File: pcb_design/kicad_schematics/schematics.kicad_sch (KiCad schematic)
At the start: 10 parts, among them IC1 PIC24FJ64GA702-I_SO

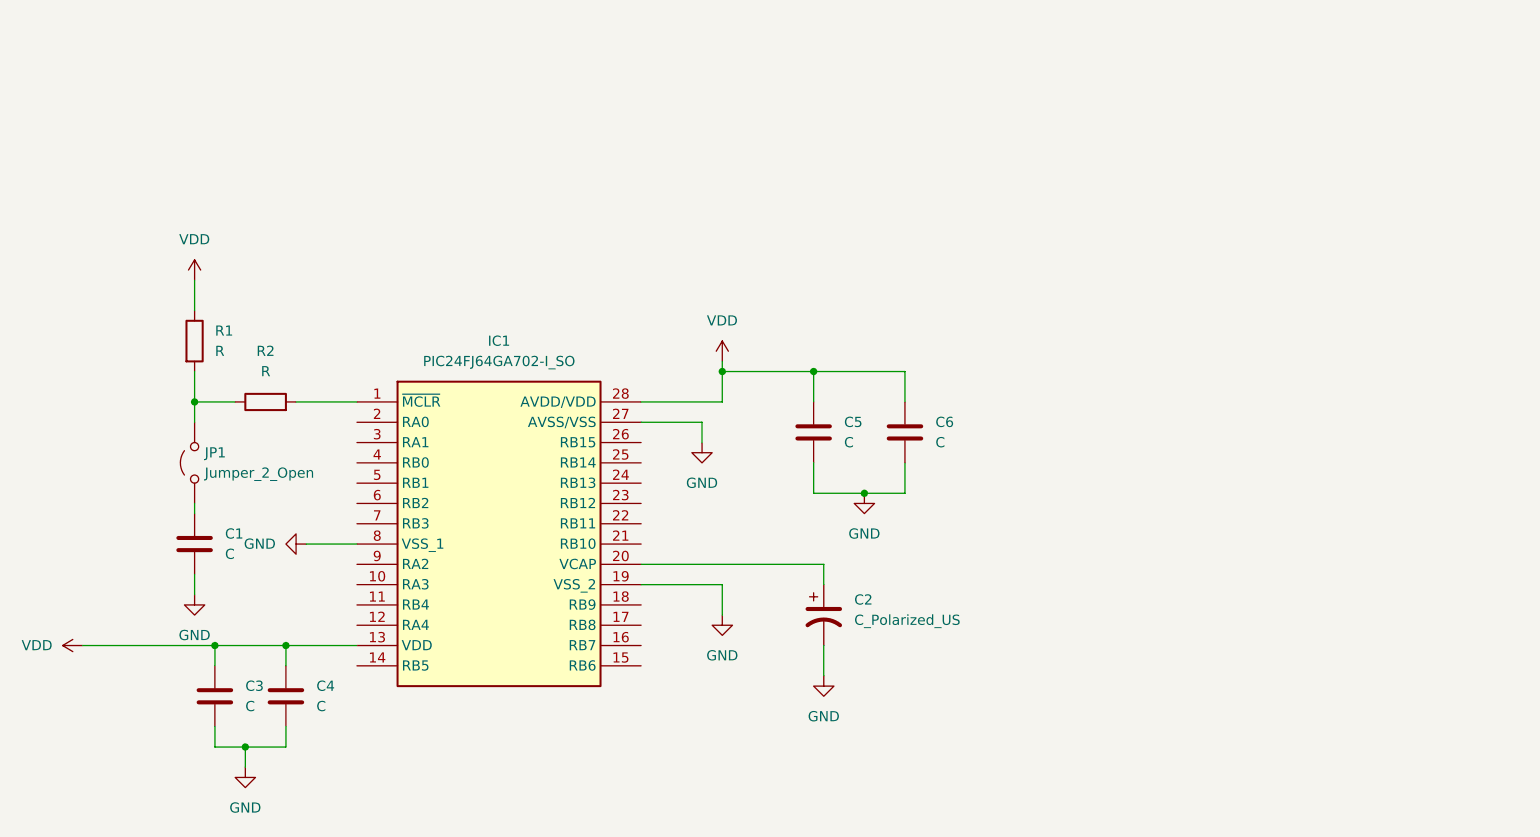
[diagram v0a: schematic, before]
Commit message: Dodani odgovarajuci kondezatori u schematics.
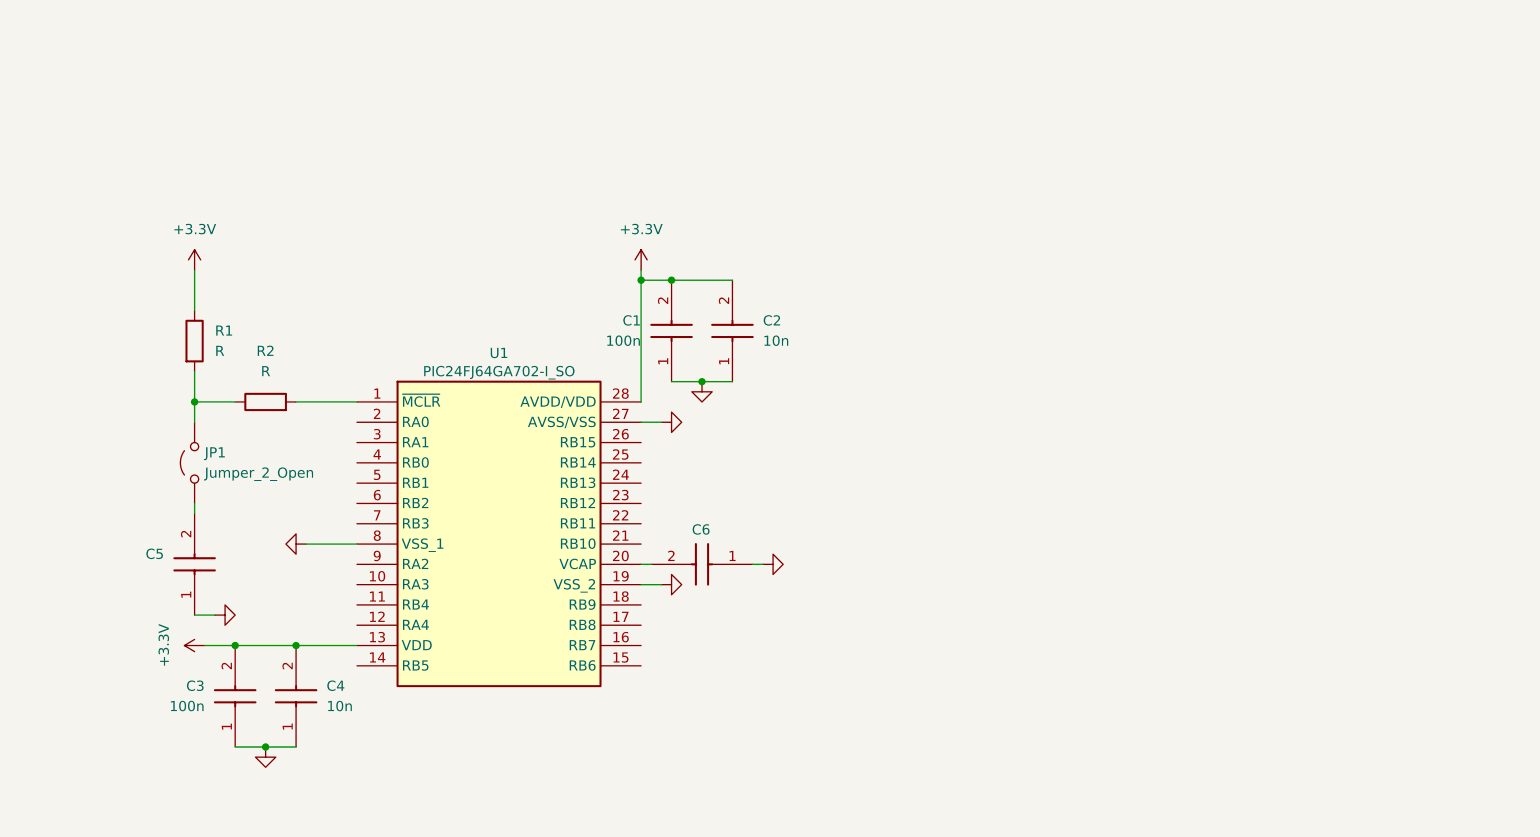
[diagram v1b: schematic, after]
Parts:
- removed C1, C3, C4, C5, C6: C, symbol Device:C
- removed C2: C_Polarized_US, symbol Device:C_Polarized_US
- added C1, C3: 100n, C0805, symbol C0805C106M4PACTU:C0805C106M4PACTU
- added C2, C4: 10n, C0805, symbol C0805C106M4PACTU:C0805C106M4PACTU
- added C5, C6: ~, C0805, symbol C0805C106M4PACTU:C0805C106M4PACTU
- renumbered IC1 to U1
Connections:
- net GND: now also C1.1, C2.1, C3.1, C4.1, C5.1, C6.1
- net at U1.20 (VCAP): now also C6.2
- net at JP1.1 (A): now also C5.2
- net VDD renamed +3.3V
- net +3.3V: now also C1.2, C2.2, C3.2, C4.2

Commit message: Dodane vrijednosti ostalih otpornika i kondenzatora u minimalnoj konf
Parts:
- C5: value ~ -> 0.1u
- C6: value ~ -> 10u
- R1: value R -> 10k
- R2: value R -> 200
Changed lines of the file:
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@@
 			)
 		)
-		(property "Value" "~"
+		(property "Value" "0.1u"
 			(at 96.52 95.2499 90)
 			(effects
@@
 			)
 		)
-		(property "Value" "R"
+		(property "Value" "200"
 			(at 109.22 69.85 90)
 			(effects
@@
 		(on_board yes)
 		(dnp no)
-		(fields_autoplaced yes)
 		(property "Reference" "#PWR07"
 			(at 105.41 104.14 0)
@@
 		)
 		(property "Value" "+3.3V"
-			(at 96.52 104.14 0)
+			(at 96.52 104.14 90)
 			(effects
 				(font
@@
 			)
 		)
-		(property "Value" "~"
-			(at 165.0999 97.79 90)
+		(property "Value" "10u"
+			(at 165.0999 97.79 0)
 			(effects
 				(font
@@
 			)
 		)
-		(property "Value" "R"
+		(property "Value" "10k"
 			(at 102.87 67.3099 0)
 			(effects

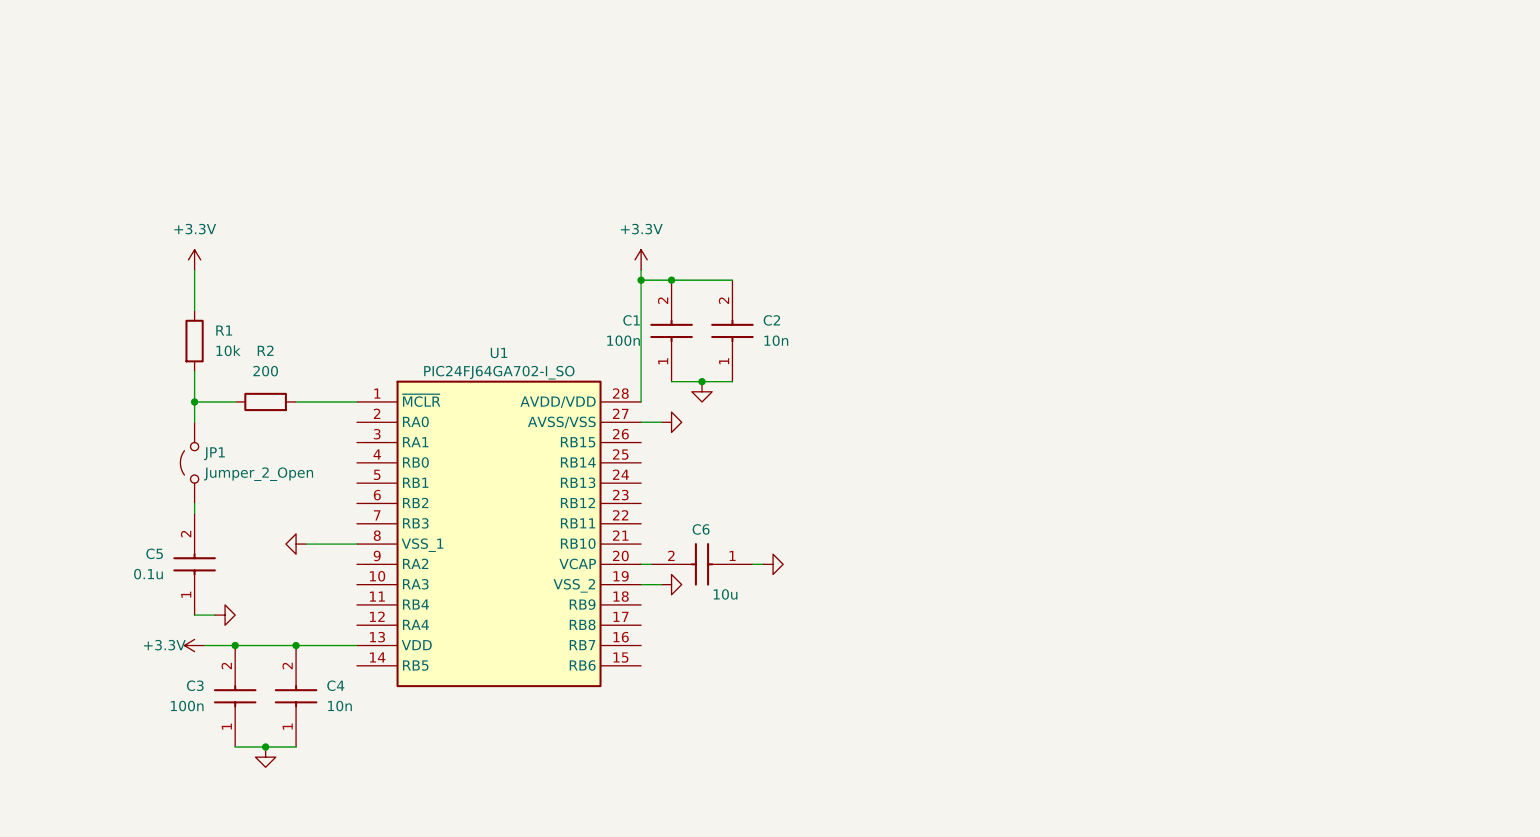
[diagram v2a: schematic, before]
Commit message: Wi-Fi modul dodan u KiCAD
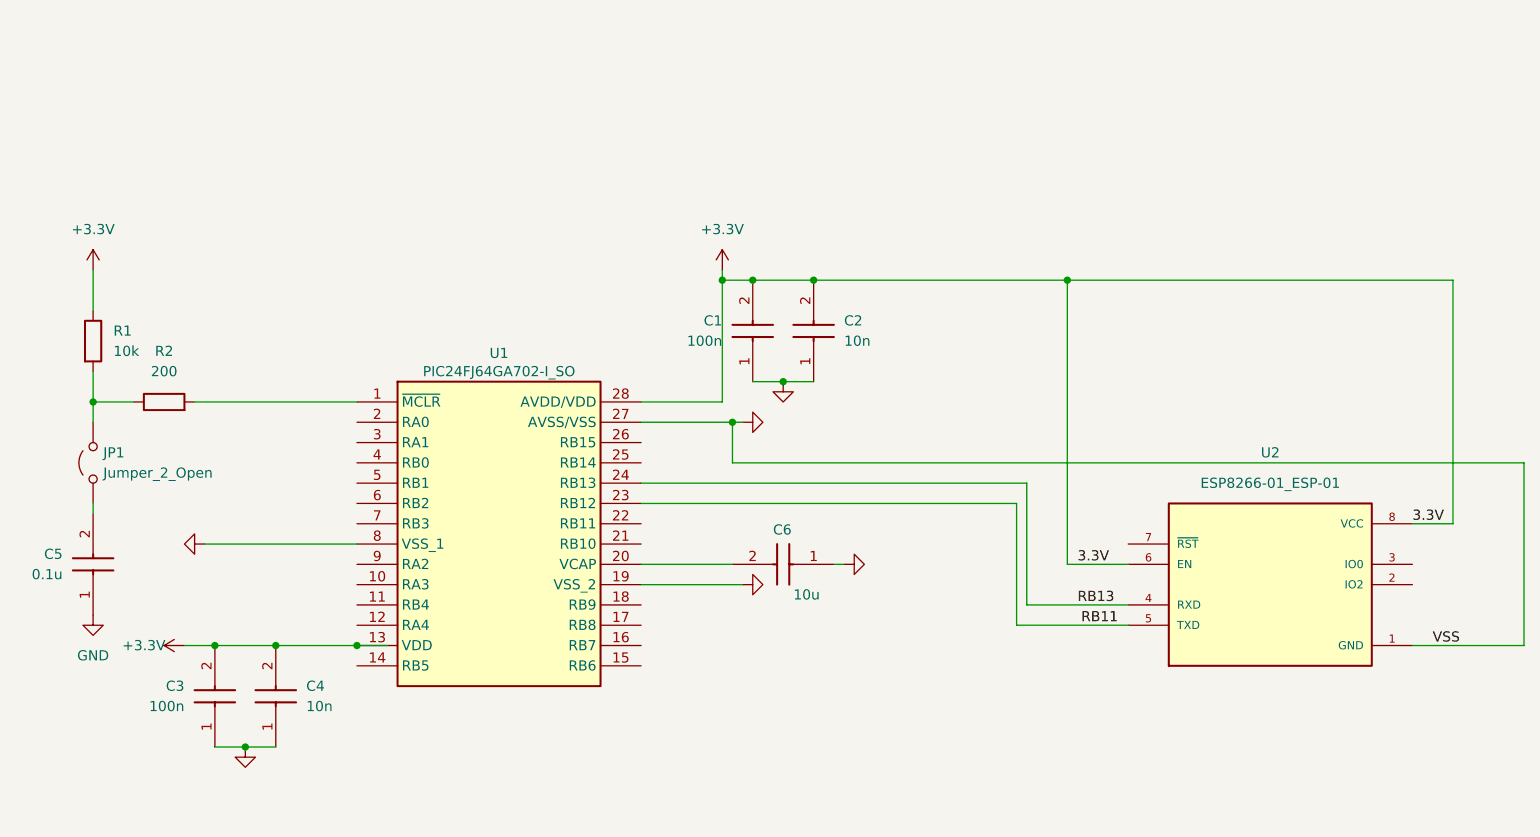
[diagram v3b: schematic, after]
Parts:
- added U2: ESP8266-01_ESP-01, ESP8266-01_ESP-01:XCVR_ESP8266-01_ESP-01, symbol ESP8266-01_ESP-01:ESP8266-01_ESP-01
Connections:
- net +3.3V: now also U2.6 (EN), U2.8 (VCC)
- net GND: now also U2.1 (GND)
- net RB11: now reaches U1.23 (RB12)
- net RB11: now also U2.5 (TXD)
- net RB13: now reaches U1.24 (RB13)
- net RB13: now also U2.4 (RXD)
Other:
- moved on the sheet: C1, C2, C3, C4, C5, C6, JP1, R1, R2

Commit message: #16 Dokumentovani modul Color 10 Click(RGB senzor) dodati u KiCad semu Izvuceni su pinovi I2C i pin za DI komunikacije
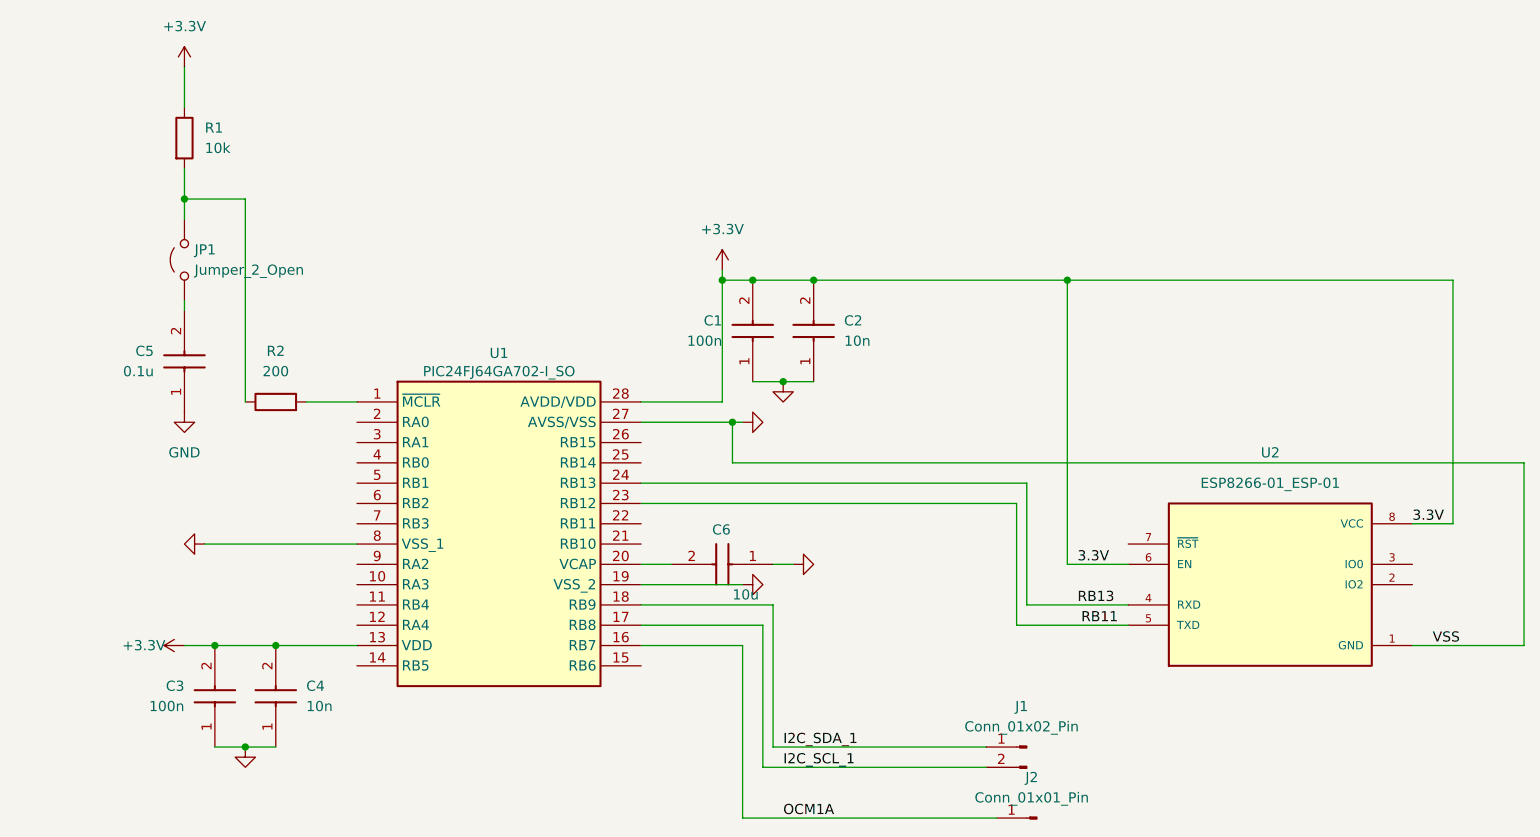
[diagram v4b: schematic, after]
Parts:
- added J1: Conn_01x02_Pin, symbol Connector:Conn_01x02_Pin
- added J2: Conn_01x01_Pin, symbol Connector:Conn_01x01_Pin
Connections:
- net OCM1A: now reaches U1.16 (RB7)
- net OCM1A: now also J2.1 (Pin_1)
- net I2C_SCL_1: now reaches U1.17 (RB8)
- net I2C_SCL_1: now also J1.2 (Pin_2)
- net I2C_SDA_1: now reaches U1.18 (RB9)
- net I2C_SDA_1: now also J1.1 (Pin_1)
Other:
- moved on the sheet: C5, C6, JP1, R1, R2
